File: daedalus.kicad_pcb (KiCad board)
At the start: 4 copper layers, 52.8 x 50.2 mm, 98 parts, among them J1 CAN Bus, J2 CAN Bus, J5 A Terminal, J6 B Terminal, J7 C Terminal, J9 USB_B_Micro, Q1 AO3401A, U1 XT30, U10 TPH, U11 TPH, U12 TPH, U13 TPH, U14 USBLC6-2SC6, U2 XT30, U3 MP2359DJ-LF-Z, U5 DRV8323RH, U6 MCP2542, U7 STM32F405RGTx, U8 TPH, U9 TPH, Y1 16MHz

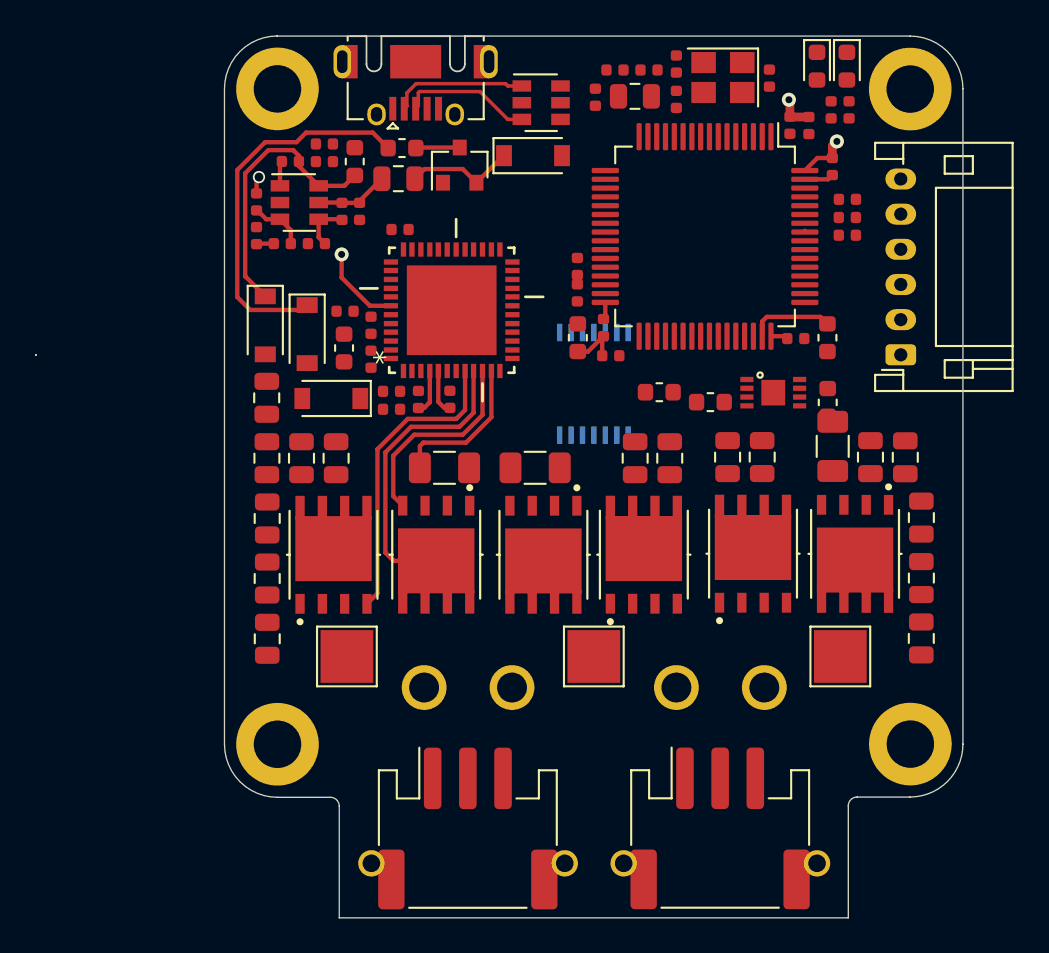
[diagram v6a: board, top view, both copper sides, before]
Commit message: Added 5V LED, finished standard routes; about to start pours
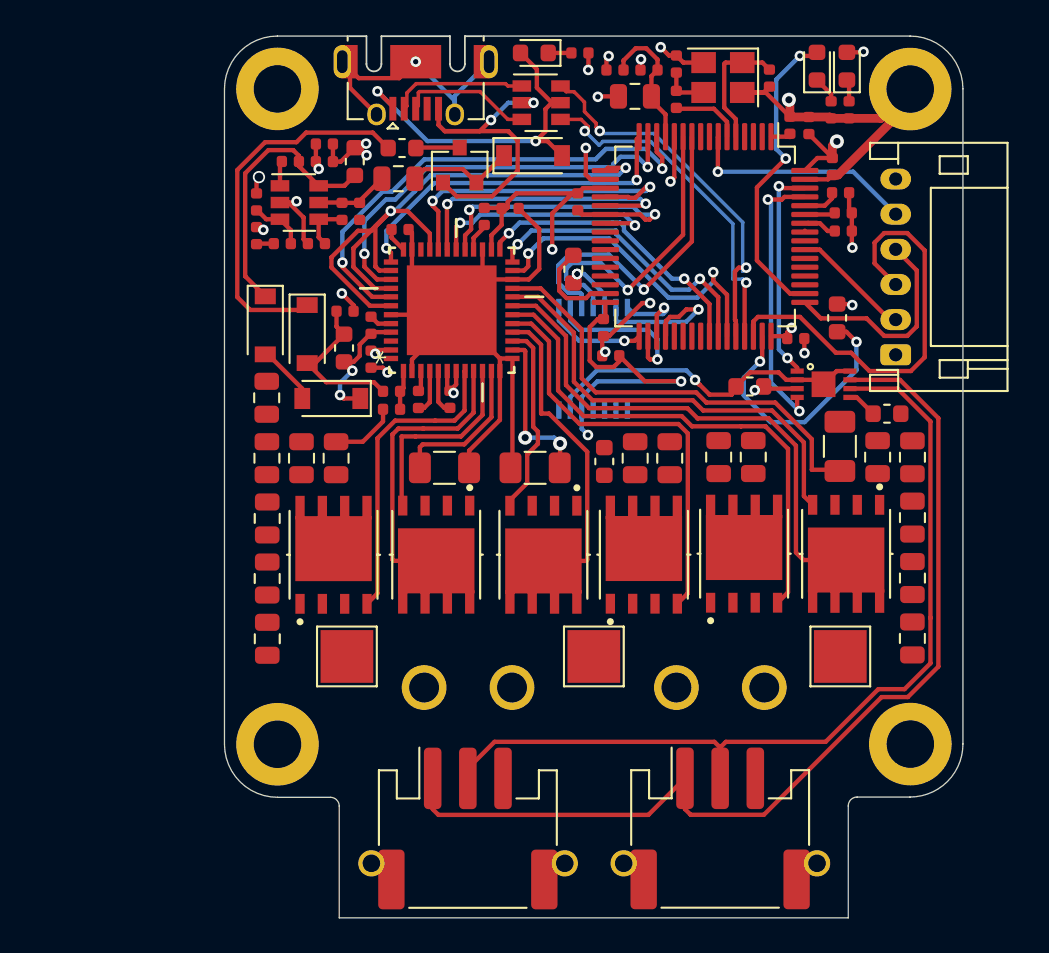
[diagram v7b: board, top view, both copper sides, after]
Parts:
- added D5: Green, LED_SMD:LED_0603_1608Metric, F.Cu at (140.6, 76.4)
- added R10: 1k5, Resistor_SMD:R_0402_1005Metric, F.Cu at (143.2, 76.4)
- moved C27 6.14 mm to (139.2, 85.2), turned to 0 degrees
- moved R6 6.04 mm to (143.0, 84.8)
- moved R7 6.01 mm to (137.7, 85.7), turned to 270 degrees
- moved C11 5.03 mm to (144.6, 99.6), turned to 270 degrees
- moved C19 3.91 mm to (142.8, 88.7)
- moved C24 3.43 mm to (160.6, 96.9), turned to 0 degrees
- moved U6 2.90 mm to (158.5, 94.5)
- moved C23 2.42 mm to (152.8, 95.3)
- moved 11 1.42 mm to (143.9, 93.8)
- moved C20 1.25 mm to (157.8, 91.4), turned to 270 degrees
- moved R15 0.54 mm to (158.0, 84.3)
- moved C38 0.51 mm to (162.1, 106.2)
- moved C41 0.51 mm to (162.1, 102.8)
- moved C28 0.51 mm to (151.1, 99.4)
- moved C31 0.51 mm to (162.1, 109.7)
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- renumbered 1 to 11
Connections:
- 11 pad 1: SPI2_CS -> SPI2_NSS
- 11 pad 2: Net-(1-Pad2) -> SPI2_SCK
- U7 pad 33: Net-(U7-Pad33) -> SPI2_NSS
- U7 pad 35: Net-(U7-Pad35) -> ENC_A
- U7 pad 36: Net-(U7-Pad36) -> ENC_B
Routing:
- net BGND: track 6.73 -> 140.0 mm, vias 1 -> 21
- net CANH: track 0.00 -> 57.0 mm
- net CANL: track 0.00 -> 50.5 mm
- net VDD: track 5.93 -> 53.5 mm, vias 2 -> 12
- net ENABLE: track 4.97 -> 39.8 mm, vias 1 -> 2
- net PHASE_C: track 0.00 -> 30.2 mm
- net GHC: track 0.00 -> 29.5 mm
- net PWM_C: track 0.00 -> 28.1 mm, vias 0 -> 2
- net SPC: track 0.00 -> 25.6 mm
- net GLC: track 0.00 -> 25.4 mm
- net SWDIO: track 0.00 -> 24.7 mm
- net GHB: track 0.00 -> 24.2 mm
- net PWM_B: track 0.00 -> 24.1 mm, vias 0 -> 2
- net USB_D-: track 0.00 -> 21.6 mm, vias 0 -> 2
- net +5V: track 0.00 -> 20.0 mm, vias 0 -> 2
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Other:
- board size 52.8 x 50.2 mm -> 42 x 50.2 mm

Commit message: Finished v3 board layout; needs fill cleanup
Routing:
- net VIN: track 4.19 -> 58.4 mm, vias 2 -> 34
- net BGND: track 140.0 -> 184.9 mm, vias 21 -> 66
- net VDD: track 53.5 -> 55.0 mm, vias 12 -> 13
- net SPB: track 9.20 -> 10.5 mm
- added copper zone on F.Cu, net BGND
- added copper zone on F.Cu, net PHASE_A
- added copper zone on F.Cu, net PHASE_B
- added copper zone on F.Cu, net PHASE_C
- added copper zone on F.Cu, net SPA
- added copper zone on F.Cu, net SPB
- added copper zone on F.Cu, net SPC
- added copper zone on B.Cu, net VIN
- added copper zone on F.Cu, net VIN
